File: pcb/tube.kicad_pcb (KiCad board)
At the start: 2 copper layers, 99.1 x 116.8 mm, 83 parts, among them J1 Screw_Terminal_01x02, J10 LED_[5..8], J11 LED_[1..4], J2 Screw_Terminal_01x02, J3 Screw_Terminal_01x02, J4 Conn_01x04_Pin, J5 Conn_01x08_Pin, J6 Conn_01x05_Pin, U1 INA226, U10 74LS32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

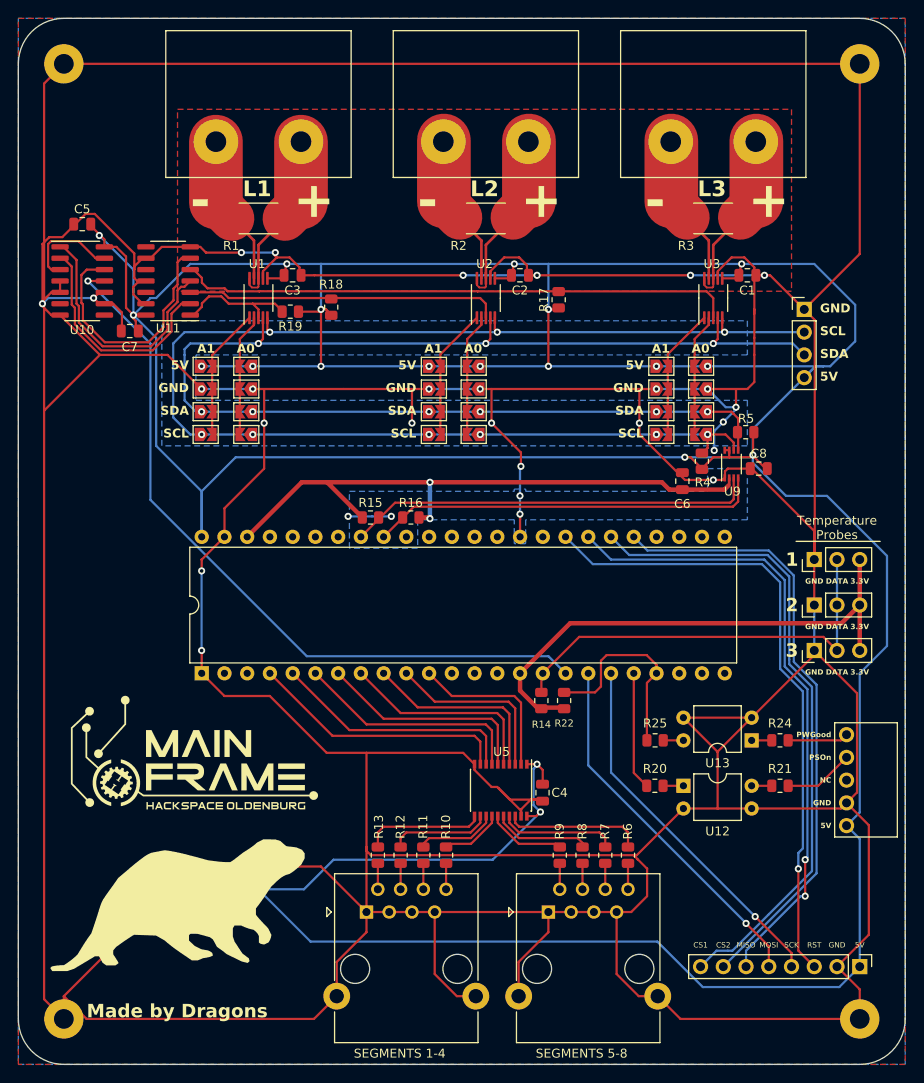
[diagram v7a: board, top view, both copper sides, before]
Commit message: PCB: Length Matching
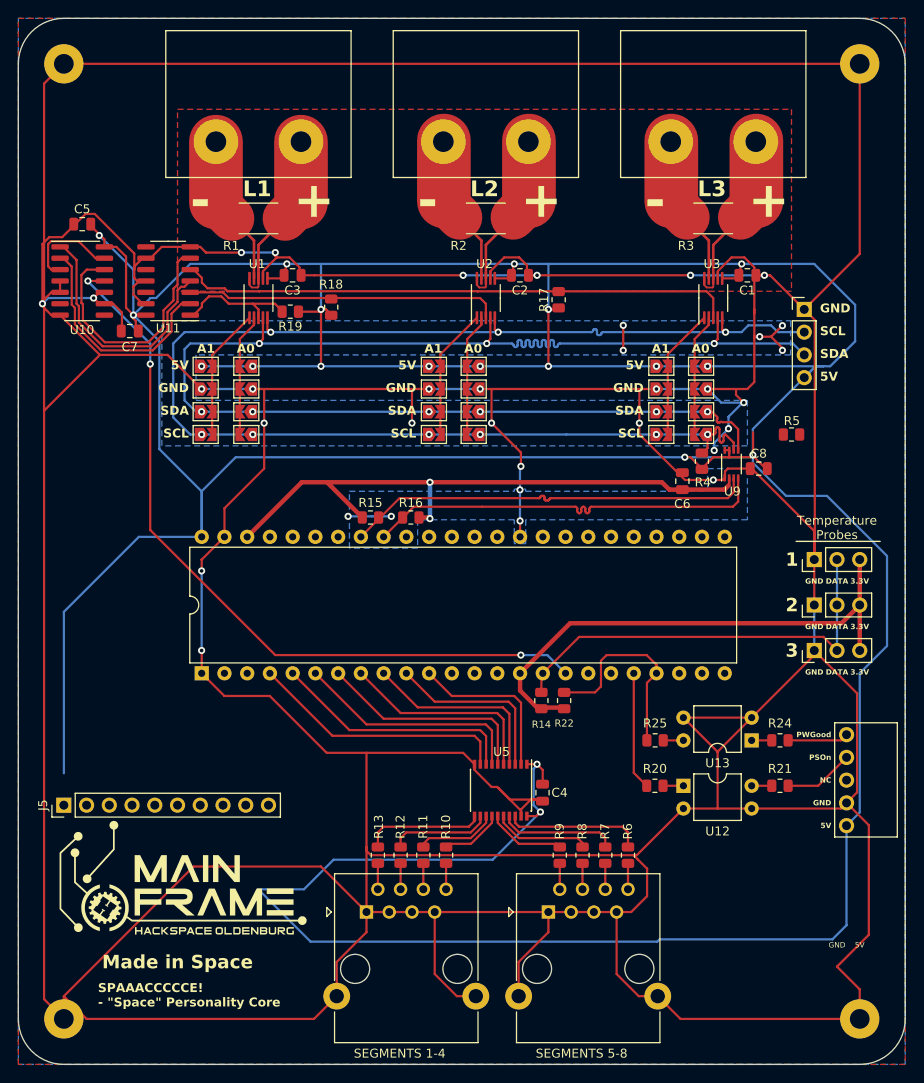
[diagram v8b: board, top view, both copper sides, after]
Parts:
- removed the REF** at (160.0, 203.2)
- J5: value Conn_01x08_Pin -> Conn_01x10_Pin; footprint Connector_PinHeader_2.54mm:PinHeader_1x08_P2.54mm_Vertical -> Connector_PinHeader_2.54mm:PinHeader_1x10_P2.54mm_Vertical
- moved J5 90.7 mm to (147.3, 192.0), turned to 90 degrees
- moved REF** 14.0 mm to (161.3, 199.4)
- moved R5 5.13 mm to (228.6, 150.6)
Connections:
- J5 pad 3: /RST -> Net-(J5-Pin_3)
- J5 pad 4: /SCK -> Net-(J5-Pin_4)
- J5 pad 5: /MOSI -> Net-(J5-Pin_5)
- J5 pad 6: /MISO -> Net-(J5-Pin_6)
- J5 pad 7: /CS2 -> Net-(J5-Pin_7)
- J5 pad 8: /CS1 -> Net-(J5-Pin_8)
- U4 pad 26: unconnected-(U4-34_RX8-Pad26) -> /CS5
- U4 pad 27: unconnected-(U4-35_TX8-Pad27) -> /CS4
- U4 pad 28: unconnected-(U4-36_CS-Pad28) -> /CS3
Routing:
- net /CS1: track 72.6 -> 0.00 mm
- net /MISO: track 71.3 -> 0.00 mm, vias 2 -> 0
- net /RST: track 71.0 -> 0.00 mm, vias 1 -> 0
- net /CS2: track 68.7 -> 0.00 mm
- net /SCK: track 41.1 -> 0.00 mm, vias 1 -> 0
- net /MOSI: track 41.1 -> 0.00 mm, vias 1 -> 0
- net +5V: track 543.4 -> 571.3 mm
- net GND: track 1016.4 -> 1026.2 mm, vias 29 -> 34
- net /SDA: track 151.2 -> 157.3 mm
- net /SCL: track 151.5 -> 155.8 mm
- net /SDA3_3: track 43.9 -> 45.9 mm
- net Net-(U4-25_A11_RX6_SDA2): track 83.6 -> 85.6 mm, vias 1 -> 3
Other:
- board text added: "Made in Space"
- board text added: "SPAAACCCCCE! - {dblquote}Space{dblquote} Personality Core"
- board text removed: "CS1"
- board text removed: "CS2"
- board text removed: "MISO"
- board text removed: "MOSI"
- board text removed: "Made by Dragons"
- board text removed: "RST"
- board text removed: "SCK"
